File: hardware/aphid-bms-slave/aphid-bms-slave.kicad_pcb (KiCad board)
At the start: 2 copper layers, 80 x 80 mm, 158 parts, among them J1 UPPER, J2 CELLS, J3 LOWER, J4 NTC3, J5 NTC2, J6 NTC1, U1 ADES1754

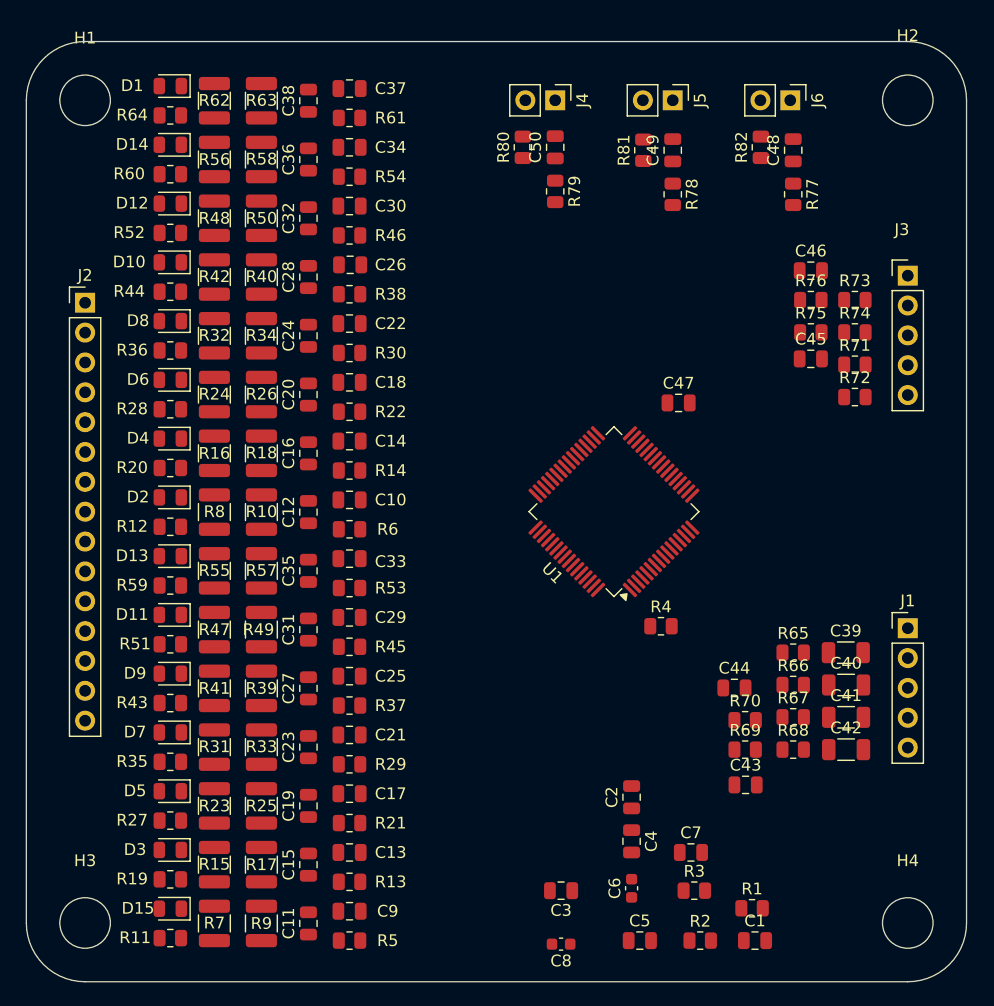
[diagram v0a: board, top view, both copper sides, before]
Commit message: Worked on BMS slave schematic and layout
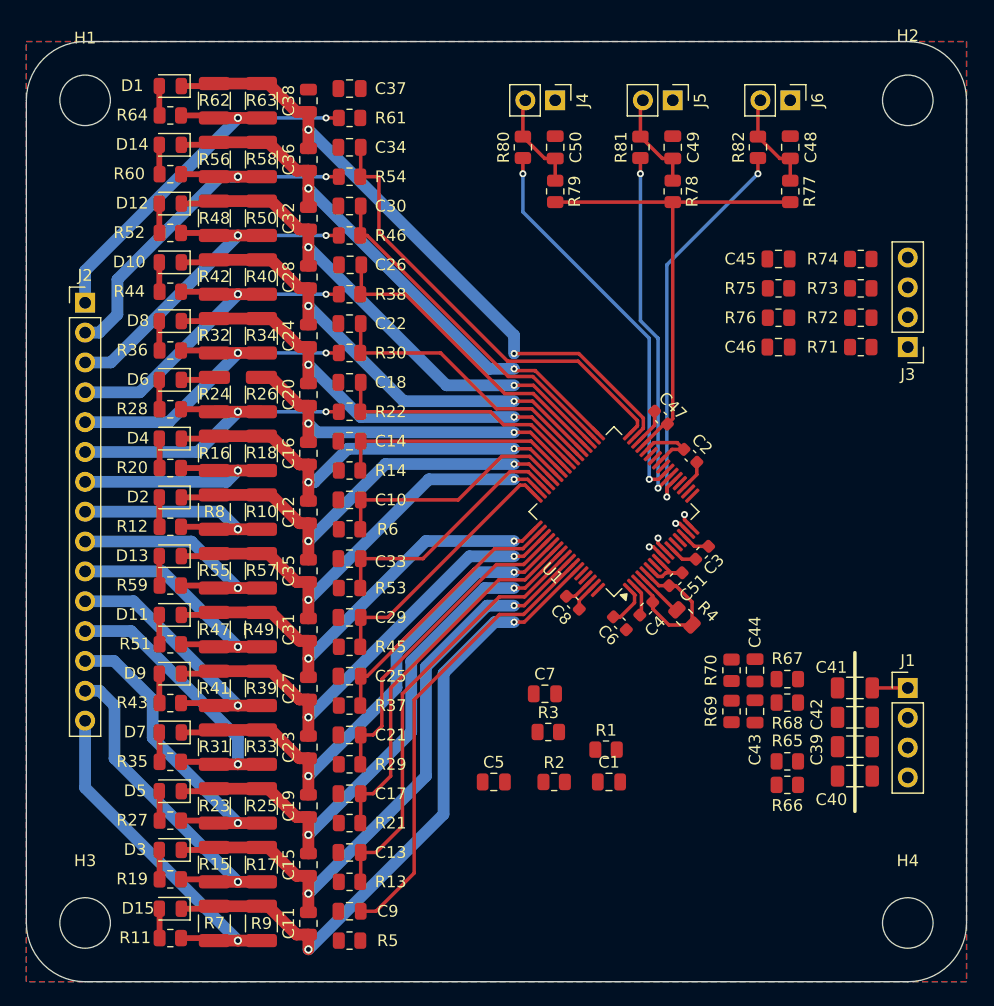
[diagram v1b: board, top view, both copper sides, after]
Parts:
- added C51: 0.47uF, Capacitor_SMD:C_0603_1608Metric, F.Cu at (107.2, 105.8)
- C2, C3, C4, C47: footprint Capacitor_SMD:C_0805_2012Metric -> Capacitor_SMD:C_0603_1608Metric
- J1, J3: footprint Connector_PinHeader_2.54mm:PinHeader_1x05_P2.54mm_Vertical -> Connector_PinHeader_2.54mm:PinHeader_1x04_P2.54mm_Vertical
- moved C3 31.2 mm to (109.5, 103.5), turned to 45 degrees
- moved C2 29.5 mm to (108.5, 95.2), turned to 135 degrees
- moved C8 29.1 mm to (98.5, 107.8), turned to 135 degrees
- moved C6 22.6 mm to (102.5, 109.5), turned to -45 degrees
- moved C4 19.8 mm to (104.8, 108.2), turned to -135 degrees
- moved R2 18.3 mm to (96.9, 123.0)
- moved R3 18.3 mm to (96.4, 118.8)
- moved C1 18.3 mm to (101.6, 123.0)
- moved C5 18.3 mm to (91.8, 123.0)
- moved C7 18.3 mm to (96.1, 115.5)
- moved R1 18.3 mm to (101.3, 120.2)
- moved R65 9.26 mm to (116.8, 121.2)
- moved C45 8.93 mm to (116.0, 78.5)
- moved R66 8.51 mm to (116.8, 123.2)
- moved C39 8.04 mm to (122.5, 120.0)
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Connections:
- J1 pad 1: /UART Isolation/ISO_ALERTIN -> /UART Isolation/ISO_RXUP
- J1 pad 2: /UART Isolation/ISO_TXUP -> /UART Isolation/ISO_RXUN
- J1 pad 3: /UART Isolation/ISO_TXUN -> /UART Isolation/ISO_TXUP
- J1 pad 4: /UART Isolation/ISO_RXUP -> /UART Isolation/ISO_TXUN
- J3 pad 1: /UART Isolation/ISO_ALERTOUT -> /UART Isolation/ISO_TXLP
- J3 pad 2: /UART Isolation/ISO_RXLP -> /UART Isolation/ISO_TXLN
- J3 pad 3: /UART Isolation/ISO_RXLN -> /UART Isolation/ISO_RXLP
- J3 pad 4: /UART Isolation/ISO_TXLP -> /UART Isolation/ISO_RXLN
- U1 pad 20: /ADES1754/ALERTOUT -> unconnected-(U1-ALERTOUT-Pad20)
- U1 pad 7: /ADES1754/ALERTIN -> unconnected-(U1-ALERTIN-Pad7)
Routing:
- net GND: track 0.00 -> 56.7 mm, vias 0 -> 2
- net /ADES1754/SW0: track 0.00 -> 56.5 mm, vias 0 -> 2
- net /ADES1754/SW14: track 0.00 -> 56.5 mm, vias 0 -> 2
- net /ADES1754/SW13: track 0.00 -> 54.3 mm, vias 0 -> 2
- net /ADES1754/SW12: track 0.00 -> 49.9 mm, vias 0 -> 2
- net /ADES1754/SW1: track 0.00 -> 48.3 mm, vias 0 -> 2
- net /ADES1754/SW2: track 0.00 -> 45.8 mm, vias 0 -> 2
- net /ADES1754/SW11: track 0.00 -> 45.7 mm, vias 0 -> 2
- net /ADES1754/SW3: track 0.00 -> 43.3 mm, vias 0 -> 2
- net /ADES1754/THRM: track 0.00 -> 42.0 mm
- net /ADES1754/SW10: track 0.00 -> 41.4 mm, vias 0 -> 2
- net /ADES1754/SW4: track 0.00 -> 40.8 mm, vias 0 -> 2
- net /ADES1754/SW8: track 0.00 -> 39.4 mm, vias 0 -> 2
- net /ADES1754/SW9: track 0.00 -> 38.9 mm, vias 0 -> 2
- net /ADES1754/C14: track 0.00 -> 38.9 mm
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- added copper zone on B.Cu, net GND
- added copper zone on F.Cu, net GND

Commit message: BMS slave 1.0 done
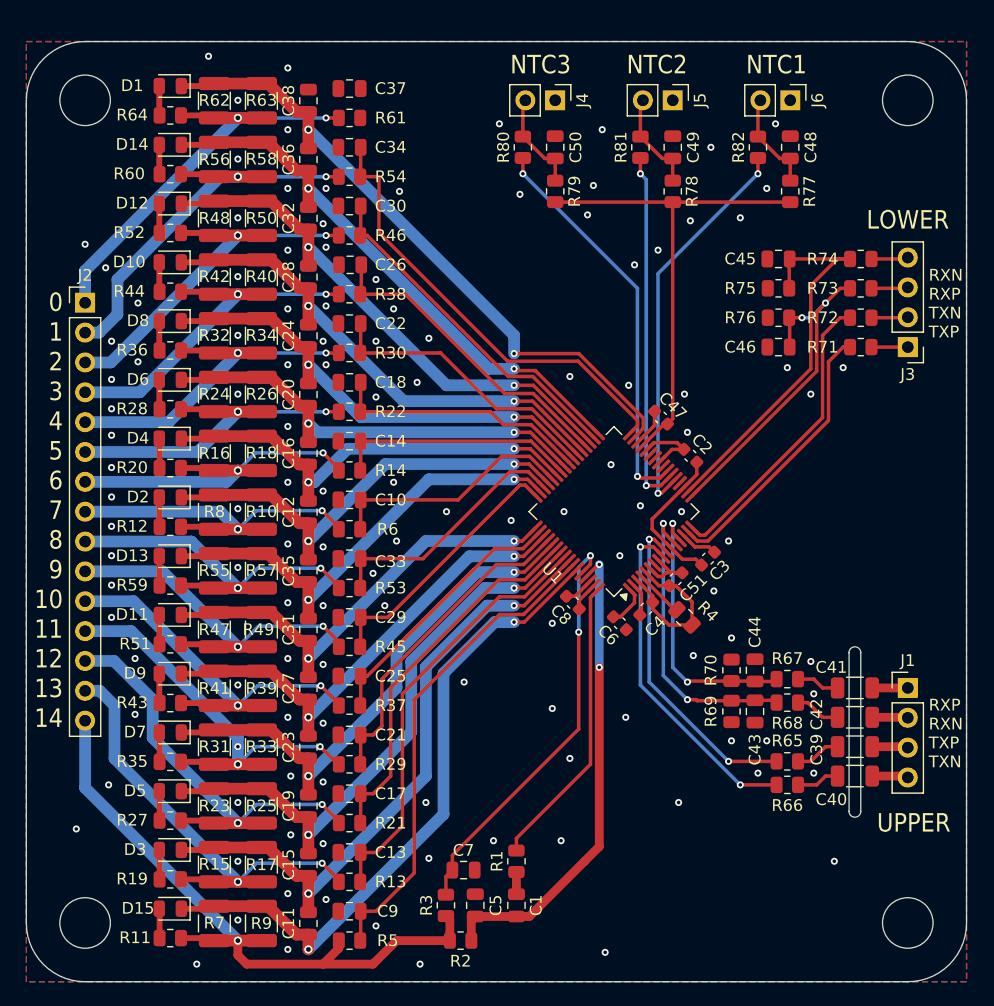
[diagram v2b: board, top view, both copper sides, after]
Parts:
- moved R3 17.1 mm to (87.7, 133.5), turned to 90 degrees
- moved C7 16.5 mm to (89.2, 130.5)
- moved R2 15.7 mm to (89.0, 136.5)
- moved C1 13.1 mm to (93.7, 133.5), turned to -90 degrees
- moved R1 12.2 mm to (93.7, 129.8), turned to 90 degrees
- moved C5 10.6 mm to (90.2, 133.5), turned to 90 degrees
- moved C3 0.71 mm to (110.0, 104.0)
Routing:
- net /ADES1754/DCIN: track 0.00 -> 40.8 mm, vias 0 -> 2
- net /ADES1754/VBLK: track 0.00 -> 35.8 mm, vias 0 -> 2
- net /ADES1754/RXLN: track 0.00 -> 33.8 mm
- net /ADES1754/RXLP: track 0.00 -> 29.8 mm, vias 0 -> 2
- net /ADES1754/TXUN: track 1.54 -> 29.1 mm, vias 1 -> 2
- net /ADES1754/TXUP: track 1.56 -> 27.8 mm, vias 1 -> 2
- net /ADES1754/RXUN: track 0.00 -> 25.8 mm, vias 0 -> 2
- net /ADES1754/CELL_TOP: track 31.0 -> 56.2 mm
- net /ADES1754/HV: track 0.00 -> 25.0 mm
- net /ADES1754/TXLN: track 1.39 -> 25.5 mm, vias 1 -> 0
- net /ADES1754/RXUP: track 0.00 -> 23.4 mm, vias 0 -> 2
- net /ADES1754/TXLP: track 1.36 -> 23.9 mm, vias 1 -> 0
- net /Cell Interface/CELL9: track 22.6 -> 32.9 mm, vias 1 -> 2
- net /Cell Interface/CELL8: track 21.6 -> 31.6 mm, vias 1 -> 2
- net /Cell Interface/CELL10: track 23.6 -> 33.7 mm, vias 1 -> 2
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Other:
- outline, holes or cut-outs redrawn
- board text added: "0 1 2 3 4 5 6 7 8 9 10 11 12 13 14"
- board text added: "LOWER"
- board text added: "NTC1"
- board text added: "NTC2"
- board text added: "NTC3"
- board text added: "RXN RXP TXN TXP"
- board text added: "RXP RXN TXP TXN"
- board text added: "UPPER"
